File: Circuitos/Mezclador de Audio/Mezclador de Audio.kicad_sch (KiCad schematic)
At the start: 98 parts, among them J1 XLR3, J2 AudioJack 6.35mm, J3 AudioJack 3.5mm, Q1 NPN, SW1 SW_Push_DPDT, SW2 SW_Nidec_CAS-120A1, U1 ${SIM.PARAMS}, U10 ${SIM.PARAMS}, U11 ${SIM.PARAMS}, U12 ${SIM.PARAMS}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

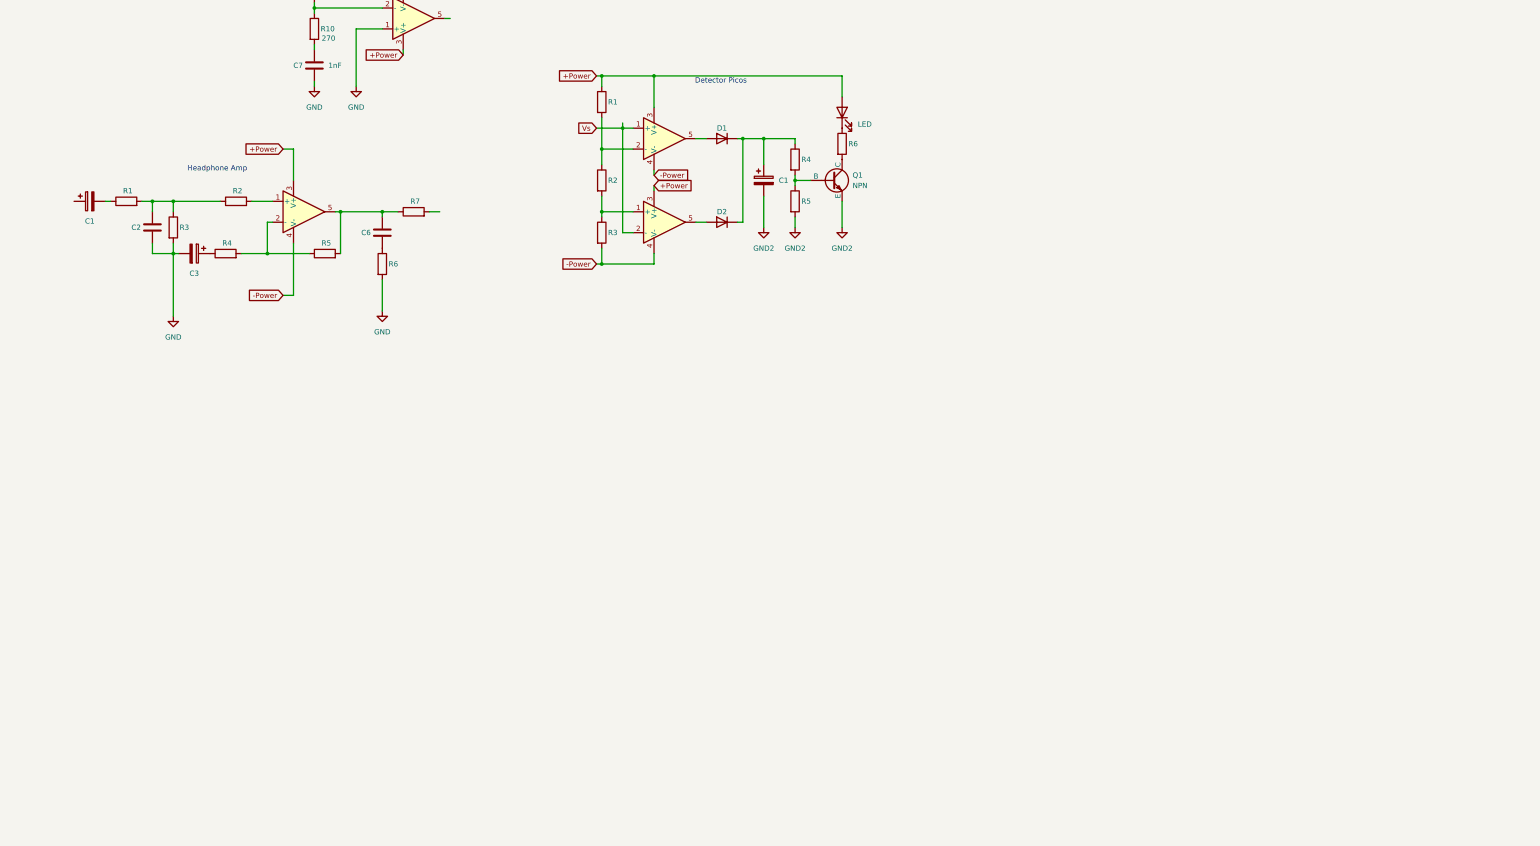
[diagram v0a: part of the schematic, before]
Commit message: Correcciones y modificaciones en fuente, amp auriculares y simul completa
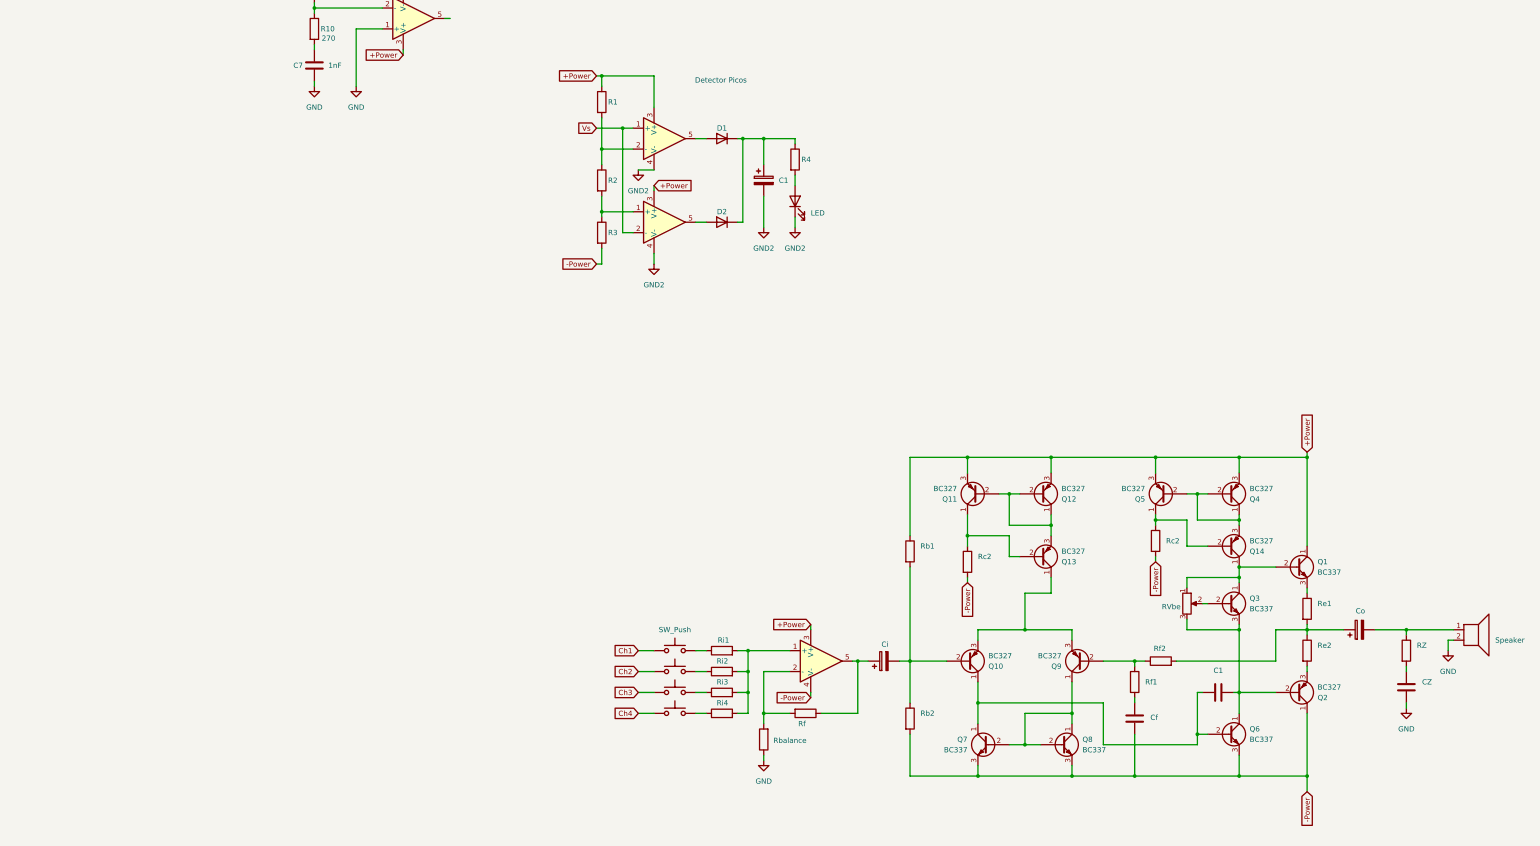
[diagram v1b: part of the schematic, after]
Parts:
- removed C1, C3: C_Polarized, symbol Device:C_Polarized
- removed C2, C6: 0.1, symbol Device:C
- removed Q1: NPN, symbol Simulation_SPICE:NPN
- removed R1, R2, R4, R5, R7: R, symbol Device:R
- removed R3, R5, R6 (x2): 24k, symbol Device:R
- added C1, CZ, Cf: C, symbol Device:C
- added Ci, Co: C_Polarized, symbol Device:C_Polarized
- added LS1: Speaker, symbol Device:Speaker
- added Q1, Q3, Q6, Q7, Q8: BC337, Package_TO_SOT_THT:TO-92_Inline, symbol Transistor_BJT:BC337
- added Q10, Q11, Q12, Q13, Q14, Q2, Q4, Q5, Q9: BC327, Package_TO_SOT_THT:TO-92_Inline, symbol Transistor_BJT:BC327
- added RVbe: R_Potentiometer, symbol Device:R_Potentiometer
- added RZ, Rb1, Rb2, Rc2 (x2), Re1, Re2, Rf1, Rf2: R, symbol Device:R
- added Rbalance, Rf, Ri1, Ri2, Ri3, Ri4: 2.7k, symbol Device:R
- added SW3, SW4, SW5, SW6: SW_Push, symbol Switch:SW_Push
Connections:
- net +Power: now also Q1.1 (C), Q11.3 (E), Q12.3 (E), Q4.3 (E), Q5.3 (E), Rb1.1; no longer D11.2 (A)
- net -Power: now also Cf.1, Q2.1 (C), Q6.3 (E), Q7.3 (E), Q8.3 (E), Rb2.2, Rc2.2, Rc2.2; no longer U11.4 (V-), U12.4 (V-)
- net Ch1: now also SW3.1
- net Ch2: now also SW4.1
- net Ch3: now also SW5.1
- net Ch4: now also SW6.1
- net GND: now also CZ.2, LS1.2, Rbalance.1
- net GND2: now also D11.1 (K), U11.4 (V-), U12.4 (V-)
- net at R4.2: now also D11.2 (A)
- net at U10.5: now also Ci.1, Rf.1
- net at U10.1 (+): now also Ri1.2, Ri2.2, Ri3.2, Ri4.2
- net at U10.2 (-): now also Rbalance.2, Rf.2
- new net: Q7.2 (B), Q8.1 (C), Q8.2 (B), Q9.1 (C)
- new net: Q9.2 (B), Rf1.1, Rf2.1
- new net: Q10.3 (E), Q13.1 (C), Q9.3 (E)
- new net: Co.1, Re1.2, Re2.1, Rf2.2
- new net: Ri4.1, SW6.2
- new net: Ri1.1, SW3.2
- new net: C1.1, Q10.1 (C), Q6.2 (B), Q7.1 (C)
- new net: Ci.2, Q10.2 (B), Rb1.2, Rb2.1
- new net: Q1.2 (B), Q14.1 (C), Q3.1 (C), RVbe.1
- new net: Q14.2 (B), Q5.1 (C), Rc2.1
- new net: Q14.3 (E), Q4.1 (C), Q4.2 (B), Q5.2 (B)
- new net: Cf.2, Rf1.2
- new net: Q11.1 (C), Q13.2 (B), Rc2.1
- new net: CZ.1, RZ.2
- new net: Q1.3 (E), Re1.1
- new net: Ri2.1, SW4.2
- new net: Q2.3 (E), Re2.2
- new net: C1.2, Q2.2 (B), Q3.3 (E), Q6.1 (C), RVbe.3
- new net: Q3.2 (B), RVbe.2
- new net: Ri3.1, SW5.2
- new net: Q11.2 (B), Q12.1 (C), Q12.2 (B), Q13.3 (E)
- new net: Co.2, LS1.1, RZ.1
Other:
- note removed: "Headphone Amp"
